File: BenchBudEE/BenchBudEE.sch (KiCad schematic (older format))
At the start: 0 parts

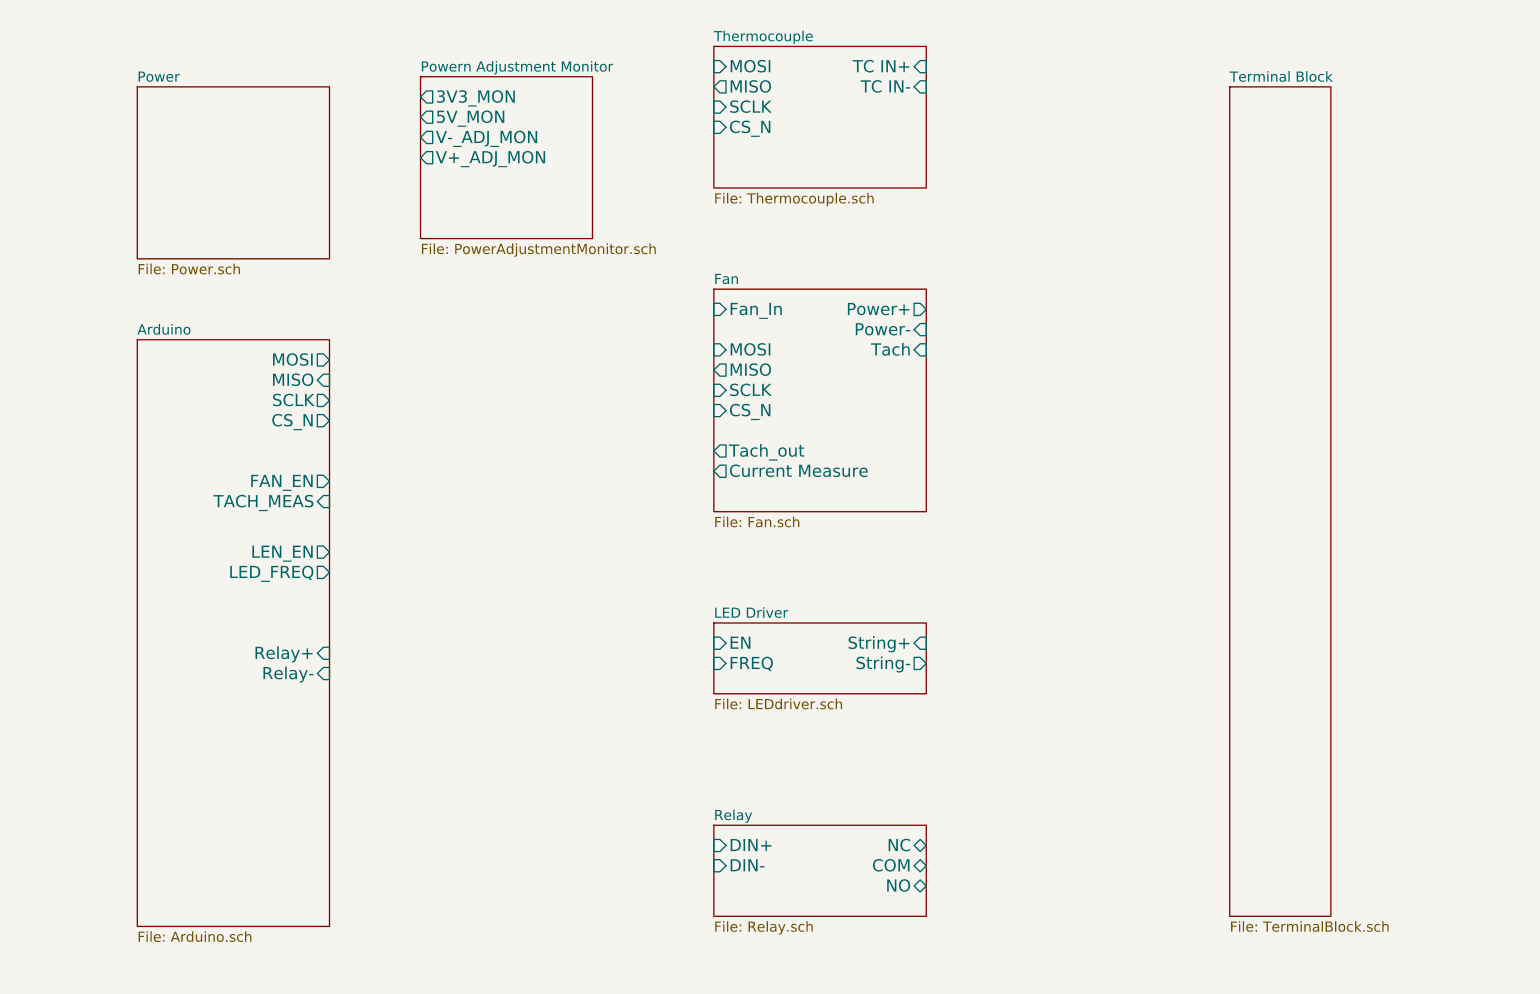
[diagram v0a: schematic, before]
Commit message: Completing schematics from week 3 videos.
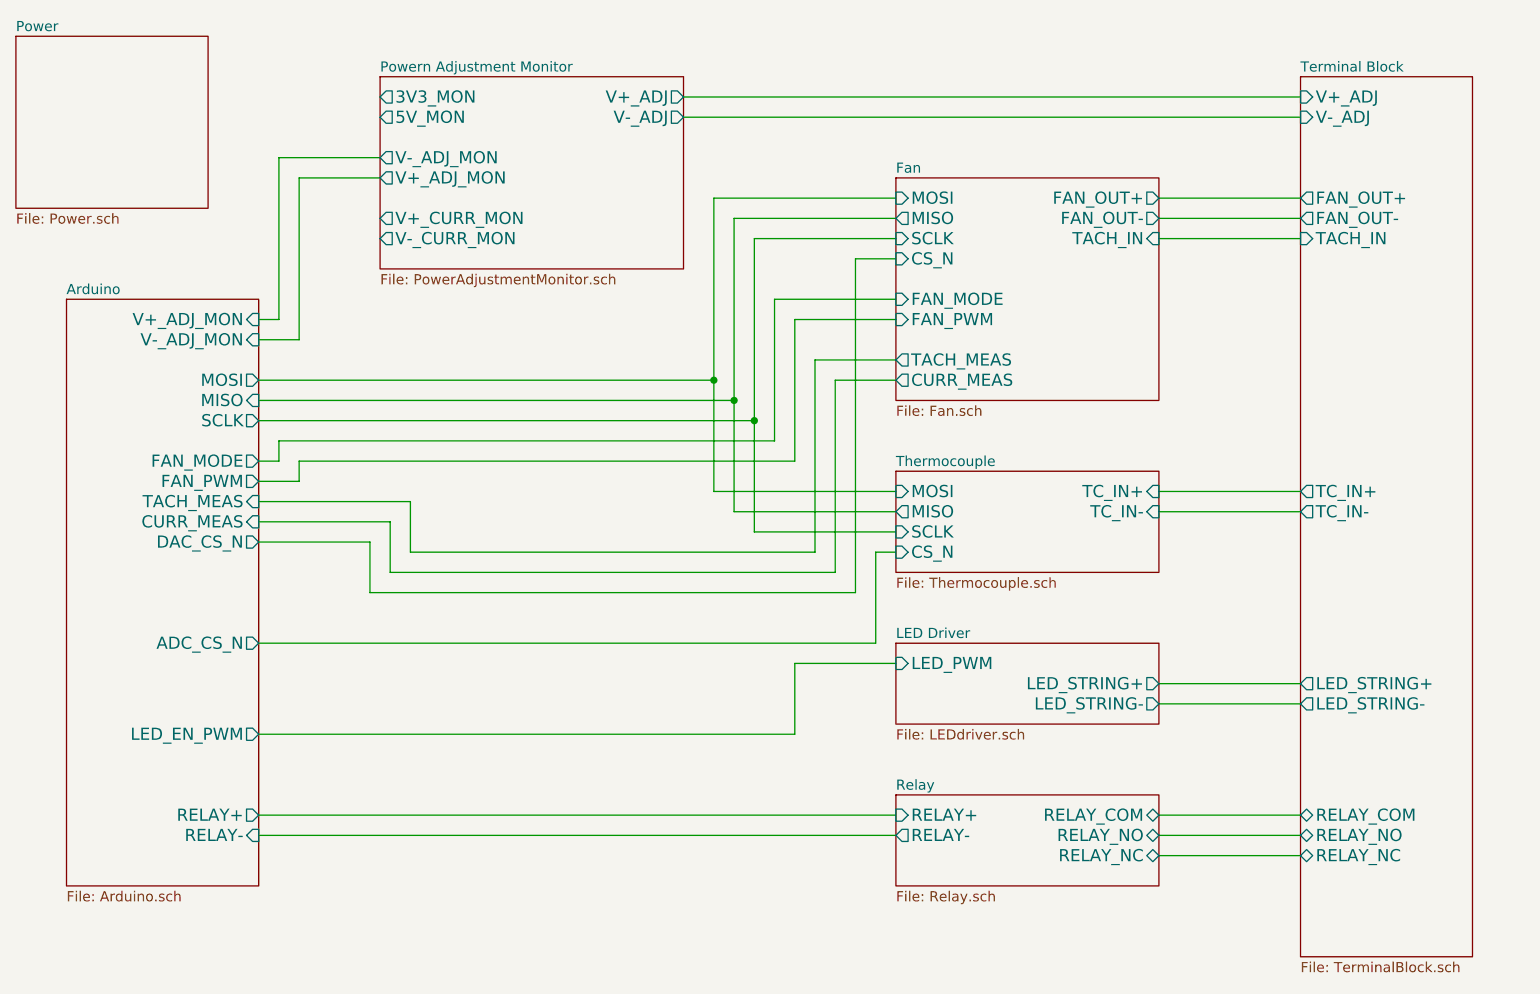
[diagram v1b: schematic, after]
